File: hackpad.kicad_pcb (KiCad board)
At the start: 2 copper layers, 32 parts, among them J1 OLED Connection, SW1 SW_Push, SW11 RotaryEncoder_Switch, SW13 RotaryEncoder_Switch, SW2 SW_Push, SW3 SW_Push, SW4 SW_Push, SW5 SW_Push, SW6 SW_Push, SW7 SW_Push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

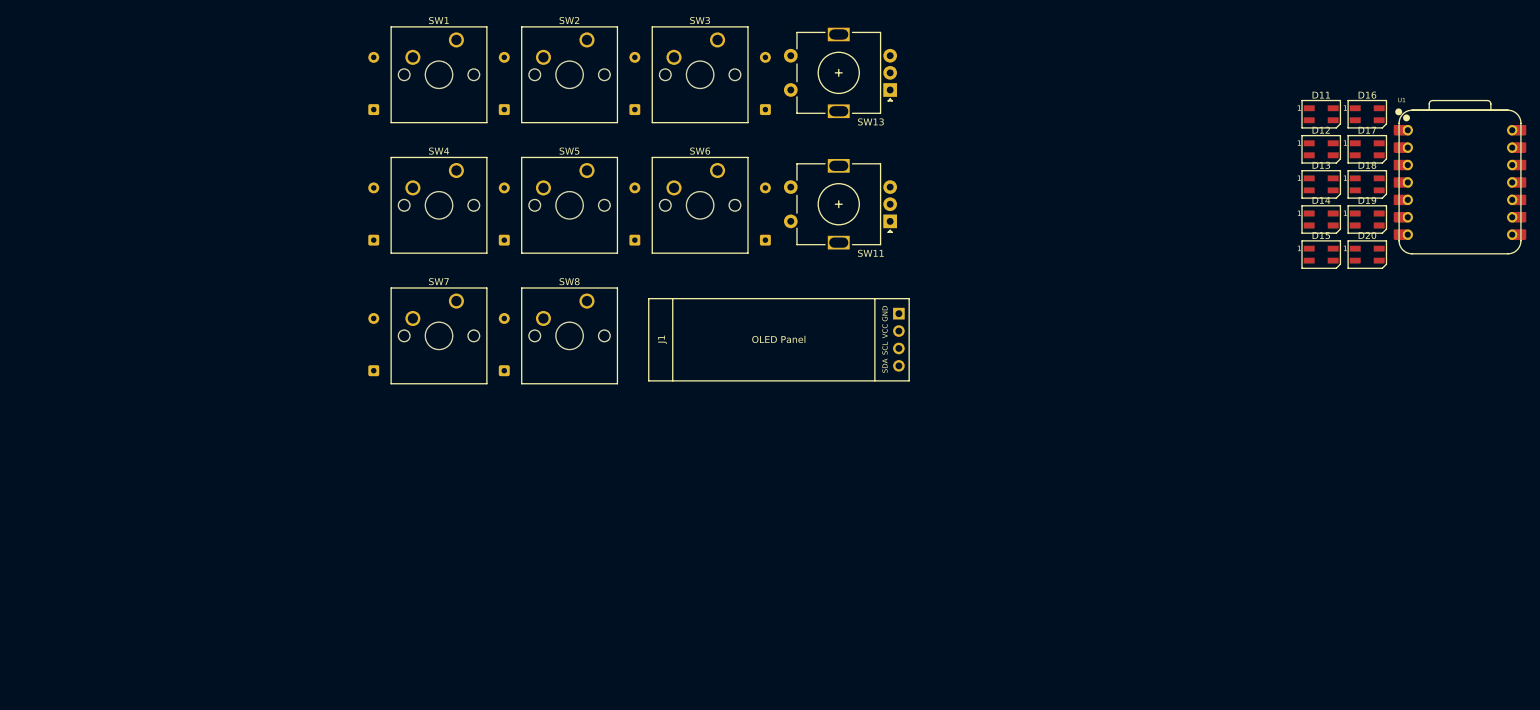
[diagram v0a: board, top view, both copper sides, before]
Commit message: finalize key and OLED screen placement
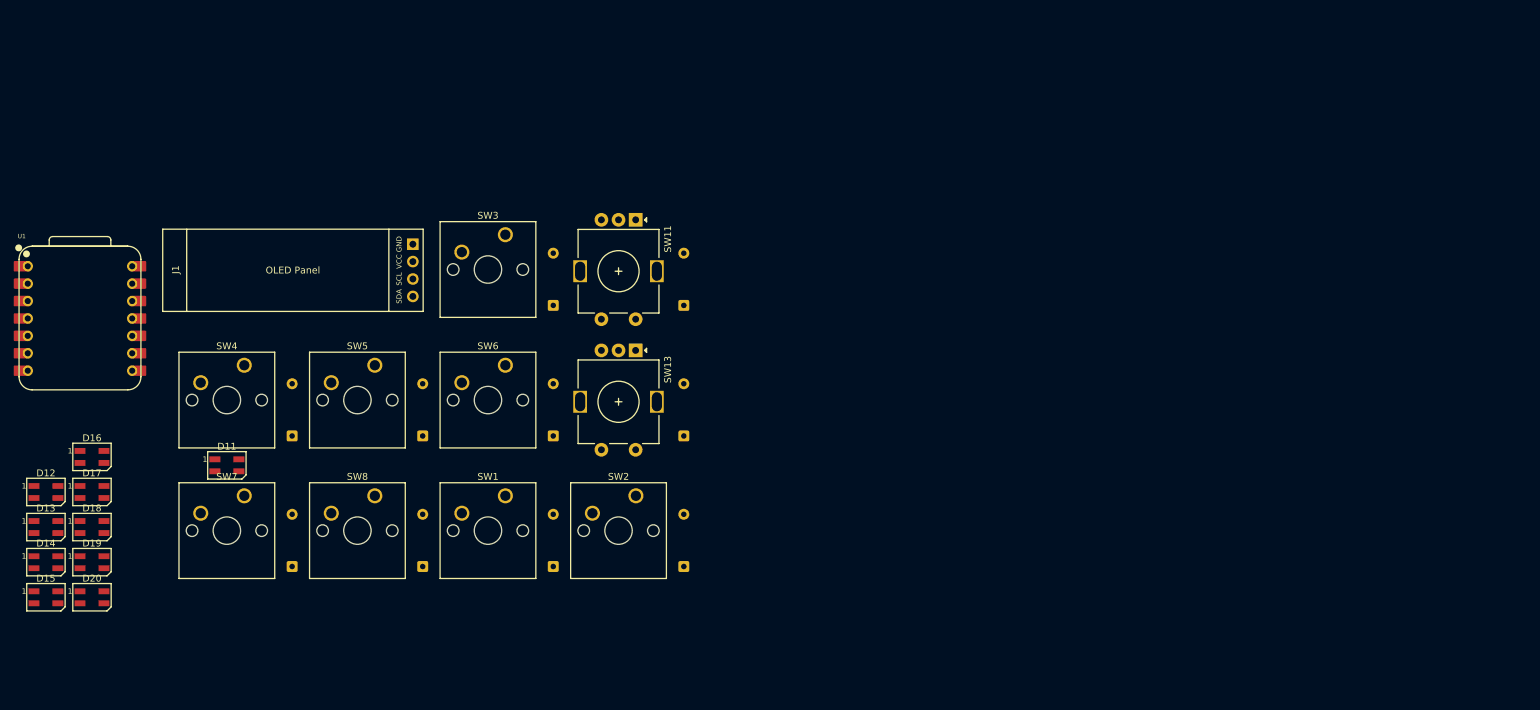
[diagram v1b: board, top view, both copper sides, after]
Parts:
- moved U1 202.3 mm to (35.7, 92.9)
- moved D12 192.7 mm to (30.7, 118.2)
- moved D13 192.7 mm to (30.7, 123.3)
- moved D14 192.7 mm to (30.7, 128.4)
- moved D15 192.7 mm to (30.7, 133.5)
- moved D16 192.7 mm to (37.5, 113.1)
- moved D17 192.7 mm to (37.5, 118.2)
- moved D18 192.7 mm to (37.5, 123.3)
- moved D19 192.7 mm to (37.5, 128.4)
- moved D20 192.7 mm to (37.5, 133.5)
- moved D11 167.7 mm to (57.1, 114.3)
- moved J1 71.6 mm to (47.8, 79.8)
- moved D1 71.6 mm to (104.8, 129.1)
- moved D2 71.6 mm to (123.8, 129.1)
- moved SW1 66.9 mm to (97.8, 118.7)
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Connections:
- D1 pad 1: Row 0 -> Row 2
- D2 pad 1: Row 0 -> Row 2
- SW1 pad 1: Column 0 -> Column 2
- SW2 pad 1: Column 1 -> Column 3

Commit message: route some pcb components
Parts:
- moved U1 102.6 mm to (138.0, 84.4)
- moved D18 81.8 mm to (114.3, 95.2)
- moved D17 76.9 mm to (114.3, 114.3)
- moved D20 69.3 mm to (95.2, 95.2)
- moved D12 66.3 mm to (95.2, 133.3)
- moved D11 60.2 mm to (114.3, 133.3)
- moved D16 57.8 mm to (95.2, 114.3)
- moved D15 49.4 mm to (76.2, 114.3)
- moved D13 46.5 mm to (76.2, 133.3)
- moved D14 26.9 mm to (57.1, 133.3)
- moved D19 24.2 mm to (57.1, 114.3)
- moved SW11 10.8 mm to (107.0, 83.2), turned to 0 degrees
- moved SW13 10.8 mm to (107.0, 102.3), turned to 0 degrees
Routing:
- net Column 0: track 0.00 -> 99.2 mm
- net Column 1: track 0.00 -> 79.1 mm
- net Column 2: track 0.00 -> 71.2 mm
- net Row 2: track 0.00 -> 57.2 mm
- net Row 1: track 0.00 -> 57.2 mm
- net Column 3: track 0.00 -> 44.0 mm
- net Row 0: track 0.00 -> 19.0 mm
- net Net-(D2-A): track 0.00 -> 13.4 mm
- net Net-(D6-A): track 0.00 -> 13.4 mm
- net Net-(D3-A): track 0.00 -> 13.4 mm
- net Net-(D1-A): track 0.00 -> 13.4 mm
- net Net-(D8-A): track 0.00 -> 13.4 mm
- net Net-(D7-A): track 0.00 -> 13.4 mm
- net Net-(D5-A): track 0.00 -> 13.4 mm
- net Net-(D4-A): track 0.00 -> 13.4 mm
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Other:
- board outline added: 104.8 x 61.9 mm

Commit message: finish pcb
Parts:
- removed D10, D9: 1N4148, Diode_THT:D_DO-35_SOD27_P7.62mm_Horizontal
- removed D12, D13, D14, D15, D16, D17, D18, D19, D20: SK6812MINI, LED_SMD:LED_SK6812MINI_PLCC4_3.5x3.5mm_P1.75mm
- removed SW13: RotaryEncoder_Switch, Rotary_Encoder:RotaryEncoder_Alps_EC11E-Switch_Vertical_H20mm
- removed U1: XIAO-RP2040-DIP, OPL:XIAO-RP2040-DIP
- added G***: LOGO, Images:tv2, F.Cu at (137.0, 116.0)
- added G***: LOGO, Images:tv, F.Cu at (136.9, 137.1)
- added LED1: SK6812MINI, LED_SMD:LED_SK6812MINI_PLCC4_3.5x3.5mm_P1.75mm, F.Cu at (114.3, 142.9)
- added LED2: SK6812MINI, LED_SMD:LED_SK6812MINI_PLCC4_3.5x3.5mm_P1.75mm, F.Cu at (95.2, 142.9)
- added LED3: SK6812MINI, LED_SMD:LED_SK6812MINI_PLCC4_3.5x3.5mm_P1.75mm, F.Cu at (76.2, 142.9)
- added LED4: SK6812MINI, LED_SMD:LED_SK6812MINI_PLCC4_3.5x3.5mm_P1.75mm, F.Cu at (76.2, 123.8)
- added LED5: SK6812MINI, LED_SMD:LED_SK6812MINI_PLCC4_3.5x3.5mm_P1.75mm, F.Cu at (95.2, 123.8)
- added LED6: SK6812MINI, LED_SMD:LED_SK6812MINI_PLCC4_3.5x3.5mm_P1.75mm, F.Cu at (114.3, 123.8)
- added LED7: SK6812MINI, LED_SMD:LED_SK6812MINI_PLCC4_3.5x3.5mm_P1.75mm, F.Cu at (114.3, 104.4)
- added LED8: SK6812MINI, LED_SMD:LED_SK6812MINI_PLCC4_3.5x3.5mm_P1.75mm, F.Cu at (95.2, 104.8)
- added LED9: SK6812MINI, LED_SMD:LED_SK6812MINI_PLCC4_3.5x3.5mm_P1.75mm, F.Cu at (76.2, 104.8)
- added XIAO-RP2040 HERE1: XIAO-RP2040-DIP, OPL:XIAO-RP2040-DIP, F.Cu at (135.7, 77.2)
- added anime: LOGO, Images:anime, B.Cu at (127.0, 124.0)
- D11: value SK6812MINI -> 1N4148; footprint LED_SMD:LED_SK6812MINI_PLCC4_3.5x3.5mm_P1.75mm -> Diode_THT:D_DO-35_SOD27_P7.62mm_Horizontal; moved to B.Cu
- moved D2 57.9 mm to (66.7, 119.5)
- moved SW4 57.9 mm to (116.8, 109.2)
- moved SW7 57.9 mm to (116.8, 128.3)
- moved D7 39.3 mm to (104.8, 138.6)
- moved SW2 39.3 mm to (78.7, 109.2)
- moved D4 39.3 mm to (104.8, 119.5)
- moved D11 35.0 mm to (126.2, 100.5), turned to 90 degrees
- moved D1 34.3 mm to (85.7, 100.5)
- moved D6 34.3 mm to (85.7, 138.6)
- moved D3 34.3 mm to (85.7, 119.5)
- moved D5 34.3 mm to (66.7, 138.6)
- moved D8 34.3 mm to (66.7, 100.5)
- moved SW5 28.6 mm to (78.7, 128.3)
- moved SW6 28.6 mm to (97.8, 128.3)
- moved SW1 28.6 mm to (97.8, 90.2)
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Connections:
- D1 pad 1: Row 2 -> Row 0
- D11 pad 1: Net-(D11-DOUT) -> Row 0
- D11 pad 2: GND -> SW11S2
- D2 pad 1: Row 2 -> Row 1
- D3 pad 1: Row 0 -> Row 1
- D5 pad 1: Row 1 -> Row 2
- D6 pad 1: Row 1 -> Row 2
- D8 pad 1: Row 2 -> Row 0
- J1 pad 2: VCC -> +5V
- SW1 pad 1: Column 2 -> Column 1
- SW11 pad S1: Column 3 -> Column 2
- SW2 pad 1: Column 3 -> Column 0
- SW3 pad 1: Column 2 -> Column 1
- SW4 pad 1: Column 0 -> Column 2
- SW5 pad 1: Column 1 -> Column 0
- SW6 pad 1: Column 2 -> Column 1
- SW7 pad 1: Column 0 -> Column 2
- SW8 pad 1: Column 1 -> Column 0
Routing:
- net GND: track 0.00 -> 326.9 mm, vias 0 -> 7
- net +5V: track 0.00 -> 280.8 mm, vias 0 -> 3
- net Row 2: track 57.2 -> 124.1 mm, vias 0 -> 1
- net Row 0: track 19.0 -> 85.8 mm
- net LED: track 0.00 -> 63.9 mm
- net Column 3: track 44.0 -> 0.00 mm
- net SW11B: track 0.00 -> 43.7 mm, vias 0 -> 1
- net SW11A: track 0.00 -> 42.7 mm, vias 0 -> 1
- net Row 1: track 57.2 -> 96.2 mm, vias 0 -> 2
- net SCL: track 0.00 -> 30.0 mm
- net SDA: track 0.00 -> 24.9 mm
- net Net-(LED4-DOUT): track 0.00 -> 23.9 mm
- net Net-(LED5-DOUT): track 0.00 -> 23.3 mm
- net Net-(LED6-DOUT): track 0.00 -> 19.7 mm
- net Net-(LED3-DOUT): track 0.00 -> 19.2 mm
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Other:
- board size 104.8 x 61.9 mm -> 83.3 x 78.6 mm

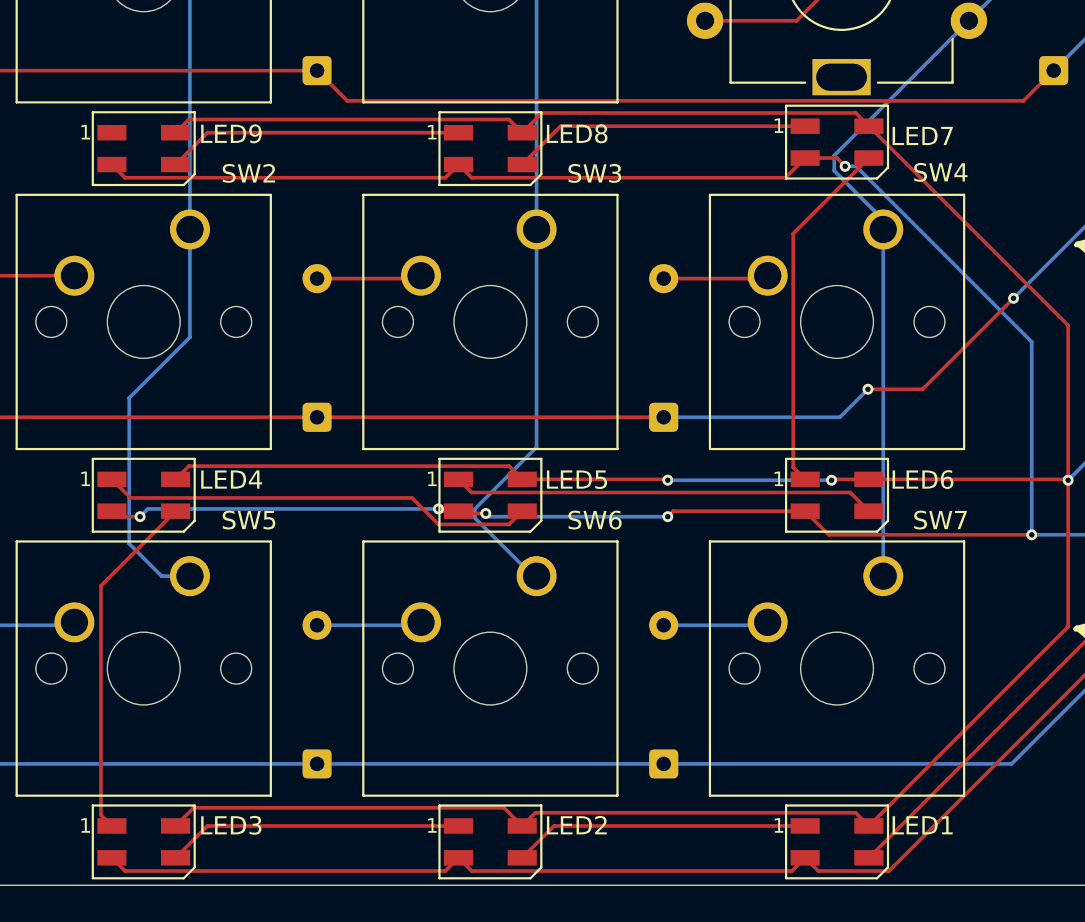
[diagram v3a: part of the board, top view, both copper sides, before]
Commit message: add 3D models for footprints
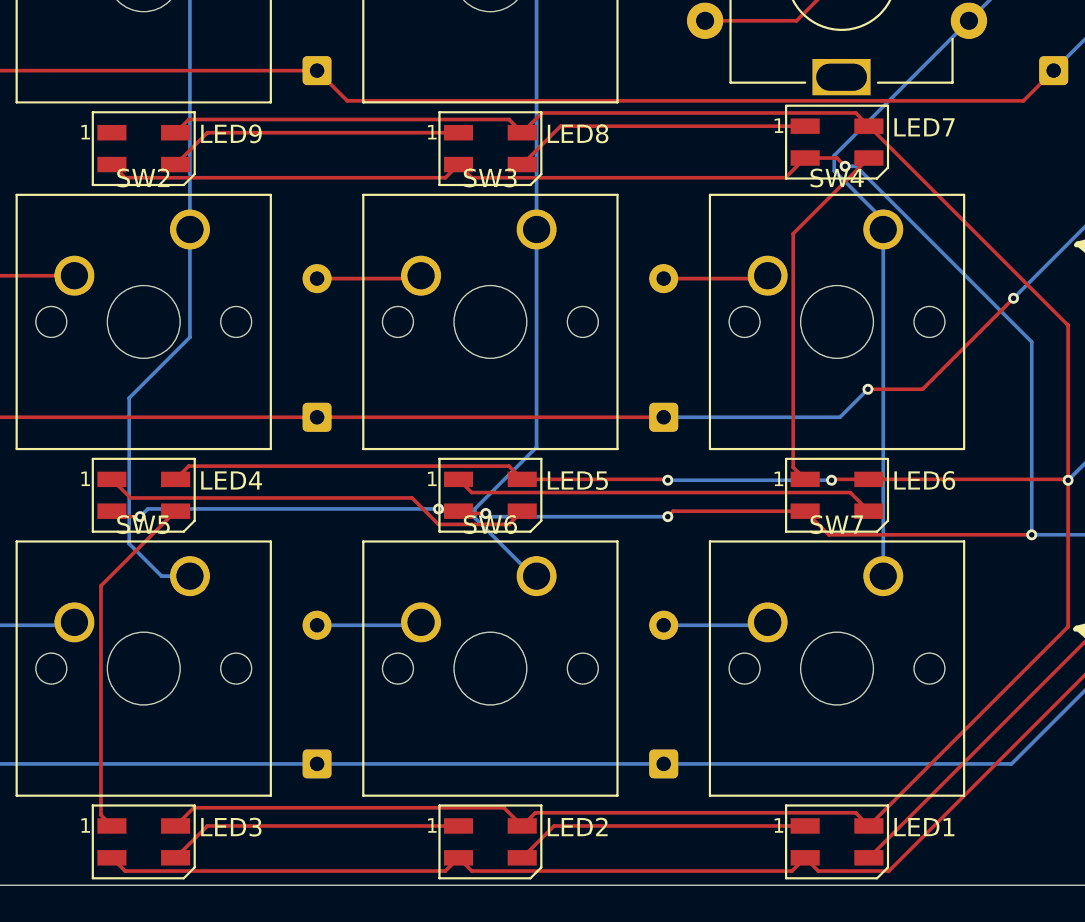
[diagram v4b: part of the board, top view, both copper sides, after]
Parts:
- J1: footprint OLED0.91:SSD1306-0.91-OLED-4pin-128x32 -> 3D_Model_Footprints:SSD1306-0.91-OLED-4pin
- LED1, LED2, LED3, LED4, LED5, LED6, LED7, LED8, LED9: footprint LED_SMD:LED_SK6812MINI_PLCC4_3.5x3.5mm_P1.75mm -> 3D_Model_Footprints:LED_SK6812MINI_PLCC4_3.5x3.5mm_P1.75mm
- SW1, SW2, SW3, SW4, SW5, SW6, SW7, SW8: footprint Button_Switch_Keyboard:SW_Cherry_MX_1.00u_PCB -> 3D_Model_Footprints:SW_Cherry_MX_1.00u_PCB_With_3D_Model
- SW11: footprint Rotary_Encoder:RotaryEncoder_Alps_EC11E-Switch_Vertical_H20mm -> 3D_Model_Footprints:RotaryEncoder_Alps_EC11E-Switch_Vertical_H20mm
- XIAO-RP2040 HERE1: footprint OPL:XIAO-RP2040-DIP -> 3D_Model_Footprints:XIAO-RP2040-DIP
